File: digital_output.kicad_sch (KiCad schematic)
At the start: 35 parts, among them J12 5 Pin 3.5mm, J6 5 Pin 3.5mm, J7 5 Pin 3.5mm, J8 5 Pin 3.5mm, K1 HF32F/xxx-Z, K2 HF32F/xxx-Z, K3 HF32F/xxx-Z, K4 HF32F/xxx-Z, U10 ULN2803A, U9 ULN2803A

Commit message: routed version
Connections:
- net Vdrive renamed VPP

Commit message: snap
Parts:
- added D46, D47, D48, D49: Red, LED_SMD:LED_0603_1608Metric, symbol Device:LED
- added J14: 5 Pin 3.5mm, Connector_Phoenix_MC:PhoenixContact_MC_1,5_5-G-3.5_1x05_P3.50mm_Horizontal, symbol Connector_Generic:Conn_01x05
- added JP7: SolderJumper_3_Bridged12, Connector_PinHeader_2.54mm:PinHeader_1x03_P2.54mm_Vertical, symbol Jumper:SolderJumper_3_Bridged12
- added R9 (x4): 100k, Resistor_SMD:R_0603_1608Metric, symbol Device:R
- added RN7: 470, Resistor_SMD:R_Array_Convex_4x0603, symbol Device:R_Pack04_Split
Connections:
- net Do0: no longer U10.8 (I8)
- net Do1: no longer U10.7 (I7)
- net Do2: no longer U10.6 (I6)
- net Do3: no longer U10.5 (I5)
- net GND: no longer U10.1 (I1), U10.2 (I2), U10.3 (I3), U10.4 (I4)
- net VCC: now also JP7.3 (B), RN7.1 (R1.1), RN7.2 (R2.1), RN7.3 (R3.1), RN7.4 (R4.1)
- net VPP: now also JP7.1 (A); no longer F6.1
- net z0: now also U10.15 (O4); no longer U10.11 (O8)
- net z1: now also U10.16 (O3); no longer U10.12 (O7)
- net z2: now also U10.17 (O2); no longer U10.13 (O6)
- net z3: now also U10.18 (O1); no longer U10.14 (O5)
- net at C28.2, C29.1, F6.2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: now also J14.5 (Pin_5), R9.2, R9.2, R9.2, R9.2
- new net: F6.1, JP7.2 (C)
- new net: D46.2 (A), RN7.8 (R1.2)
- new net: D49.2 (A), RN7.5 (R4.2)
- new net: D48.2 (A), RN7.6 (R3.2)
- new net: D47.2 (A), RN7.7 (R2.2)
- new net Do10: U10.6 (I6)
- new net Do11: U10.5 (I5)
- new net Do12: U10.4 (I4)
- new net Do13: U10.3 (I3)
- new net Do14: U10.2 (I2)
- new net Do15: U10.1 (I1)
- new net Do8: U10.8 (I8)
- new net Do9: U10.7 (I7)
- new net Xo10: D47.1 (K), J14.3 (Pin_3), R9.1, U10.13 (O6)
- new net Xo11: D46.1 (K), J14.4 (Pin_4), R9.1, U10.14 (O5)
- new net Xo8: D49.1 (K), J14.1 (Pin_1), R9.1, U10.11 (O8)
- new net Xo9: D48.1 (K), J14.2 (Pin_2), R9.1, U10.12 (O7)
- no-connect marks 4 -> 0

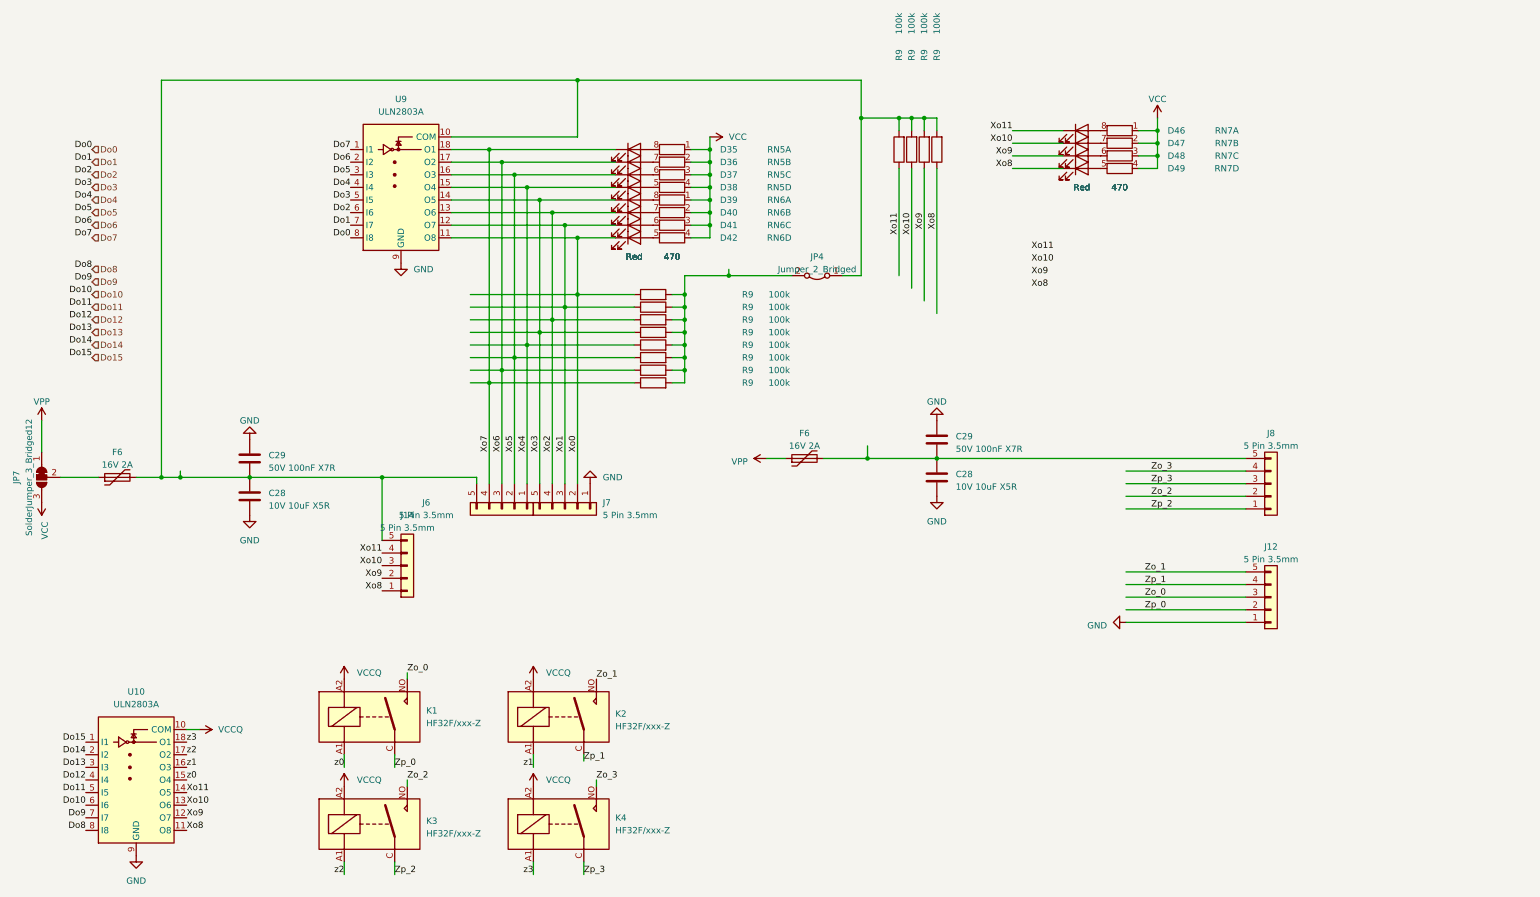
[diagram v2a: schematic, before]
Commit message: Preparation for future use.
Reworked to use i2c bus expanders.
added sketch for add-on boards.
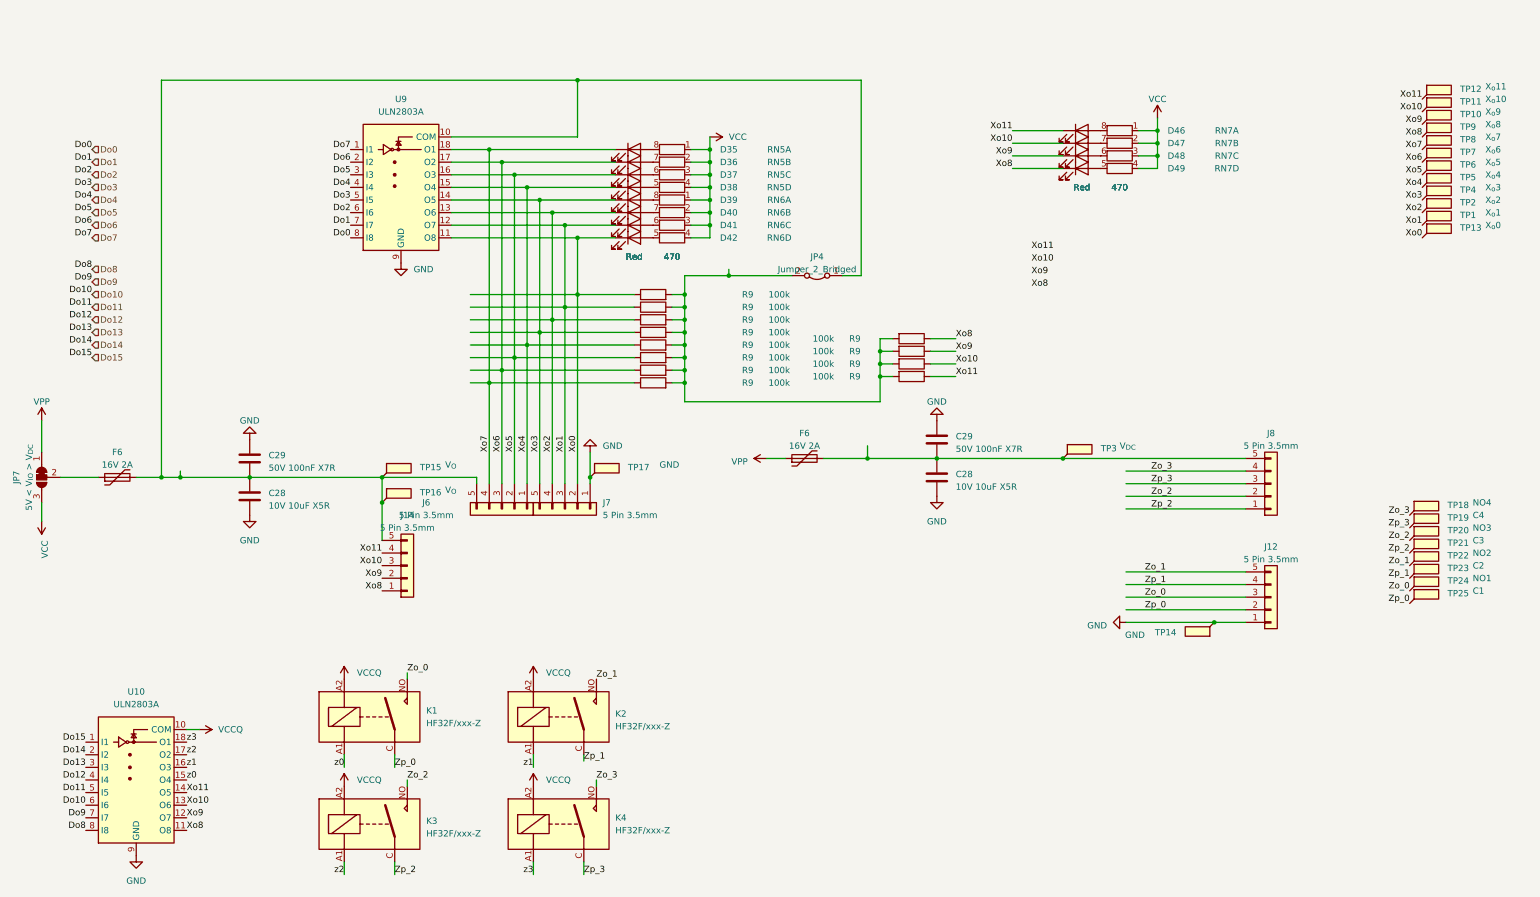
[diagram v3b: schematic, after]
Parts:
- removed R9 (x4): 100k, Resistor_SMD:R_0603_1608Metric, symbol Device:R
- added R9 (x4): 100k, Resistor_SMD:R_0603_1608Metric, symbol Device:R
- added TP1: X_{o}1, TestPoint:TestPoint_Pad_1.0x1.0mm, symbol Connector:TestPoint_Flag
- added TP10: X_{o}9, TestPoint:TestPoint_Pad_1.0x1.0mm, symbol Connector:TestPoint_Flag
- added TP11: X_{o}10, TestPoint:TestPoint_Pad_1.0x1.0mm, symbol Connector:TestPoint_Flag
- added TP12: X_{o}11, TestPoint:TestPoint_Pad_1.0x1.0mm, symbol Connector:TestPoint_Flag
- added TP13: X_{o}0, TestPoint:TestPoint_Pad_1.0x1.0mm, symbol Connector:TestPoint_Flag
- added TP14, TP17: GND, TestPoint:TestPoint_Pad_1.0x1.0mm, symbol Connector:TestPoint_Flag
- added TP15, TP16: V_{O}, TestPoint:TestPoint_Pad_1.0x1.0mm, symbol Connector:TestPoint_Flag
- added TP18: NO4, TestPoint:TestPoint_Pad_1.0x1.0mm, symbol Connector:TestPoint_Flag
- added TP19: C4, TestPoint:TestPoint_Pad_1.0x1.0mm, symbol Connector:TestPoint_Flag
- added TP2: X_{o}2, TestPoint:TestPoint_Pad_1.0x1.0mm, symbol Connector:TestPoint_Flag
- added TP20: NO3, TestPoint:TestPoint_Pad_1.0x1.0mm, symbol Connector:TestPoint_Flag
- added TP21: C3, TestPoint:TestPoint_Pad_1.0x1.0mm, symbol Connector:TestPoint_Flag
- added TP22: NO2, TestPoint:TestPoint_Pad_1.0x1.0mm, symbol Connector:TestPoint_Flag
- added TP23: C2, TestPoint:TestPoint_Pad_1.0x1.0mm, symbol Connector:TestPoint_Flag
- added TP24: NO1, TestPoint:TestPoint_Pad_1.0x1.0mm, symbol Connector:TestPoint_Flag
- added TP25: C1, TestPoint:TestPoint_Pad_1.0x1.0mm, symbol Connector:TestPoint_Flag
- added TP3: V_{DC}, TestPoint:TestPoint_Pad_1.0x1.0mm, symbol Connector:TestPoint_Flag
- added TP4: X_{o}3, TestPoint:TestPoint_Pad_1.0x1.0mm, symbol Connector:TestPoint_Flag
- added TP5: X_{o}4, TestPoint:TestPoint_Pad_1.0x1.0mm, symbol Connector:TestPoint_Flag
- added TP6: X_{o}5, TestPoint:TestPoint_Pad_1.0x1.0mm, symbol Connector:TestPoint_Flag
- added TP7: X_{o}6, TestPoint:TestPoint_Pad_1.0x1.0mm, symbol Connector:TestPoint_Flag
- added TP8: X_{o}7, TestPoint:TestPoint_Pad_1.0x1.0mm, symbol Connector:TestPoint_Flag
- added TP9: X_{o}8, TestPoint:TestPoint_Pad_1.0x1.0mm, symbol Connector:TestPoint_Flag
- JP7: value SolderJumper_3_Bridged12 -> 5V < V_{IO} > V_{DC}
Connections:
- net GND: now also TP14.1, TP17.1
- net Xo0: now also TP13.1
- net Xo1: now also TP1.1
- net Xo10: now also R9.1, TP11.1
- net Xo11: now also R9.1, TP12.1
- net Xo2: now also TP2.1
- net Xo3: now also TP4.1
- net Xo4: now also TP5.1
- net Xo5: now also TP6.1
- net Xo6: now also TP7.1
- net Xo7: now also TP8.1
- net Xo8: now also R9.1, TP9.1
- net Xo9: now also R9.1, TP10.1
- net Zo_0: now also TP24.1
- net Zo_1: now also TP22.1
- net Zo_2: now also TP20.1
- net Zo_3: now also TP18.1
- net Zp_0: now also TP25.1
- net Zp_1: now also TP23.1
- net Zp_2: now also TP21.1
- net Zp_3: now also TP19.1
- net at C28.2, C29.1, F6.2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: now also TP15.1, TP16.1
- net at JP4.2 (B), R9.2, R9.2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: now also R9.2, R9.2, R9.2, R9.2
- net at C28.2, C29.1, F6.2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: now also TP3.1
